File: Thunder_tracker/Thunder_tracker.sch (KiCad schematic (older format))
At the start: 5 parts, among them U1 ATmega8A-PU, U2 RFM95W-868S2

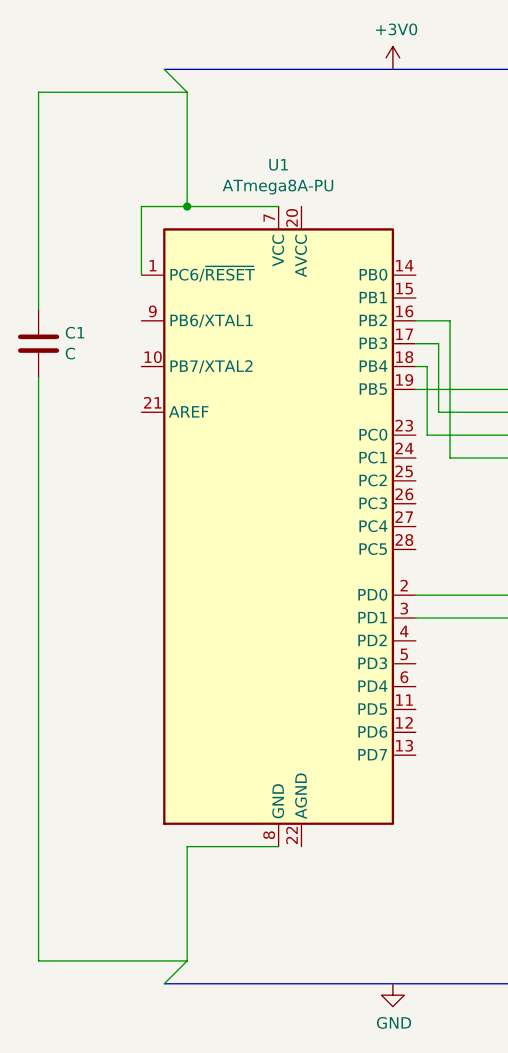
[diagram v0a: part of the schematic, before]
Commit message: Updated schematics. Now we'll use an external 32.768KHz crystal.
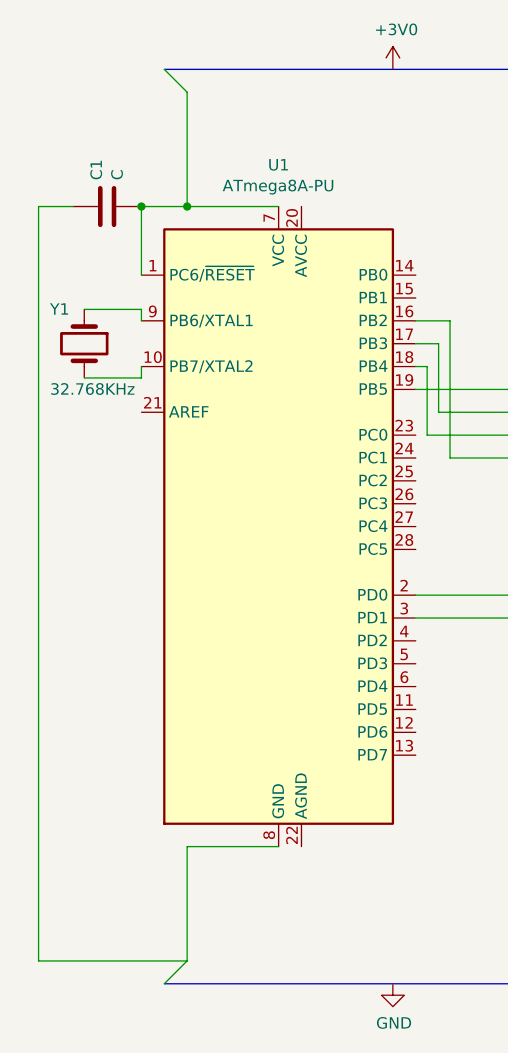
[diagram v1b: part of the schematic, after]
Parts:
- added Y1: 32.768KHz, symbol Device:Crystal
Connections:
- net at U1.1 (PC6/~RESET), U1.7 (VCC): now also C1.2; no longer C1.1
- net at U1.10 (PB7/XTAL2): now also Y1.2
- net at U1.8 (GND): now also C1.1; no longer C1.2
- net at U1.9 (PB6/XTAL1): now also Y1.1
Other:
- moved on the sheet: C1
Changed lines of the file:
@@
 L Device:C C1
 U 1 1 5D9B5CBD
-P 3000 2050
-F 0 "C1" H 3115 2096 50  0000 L CNN
-F 1 "C" H 3115 2005 50  0000 L CNN
-F 2 "" H 3038 1900 50  0001 C CNN
-F 3 "~" H 3000 2050 50  0001 C CNN
-	1    3000 2050
-	1    0    0    -1
+P 3300 1450
+F 0 "C1" H 3415 1496 50  0000 L CNN
+F 1 "C" H 3415 1405 50  0000 L CNN
+F 2 "" H 3338 1300 50  0001 C CNN
+F 3 "~" H 3300 1450 50  0001 C CNN
+	1    3300 1450
+	0    -1   -1   0
 $EndComp
 Wire Wire Line
-	3000 2200 3000 4750
-Wire Wire Line
 	3000 4750 3650 4750
-Wire Wire Line
-	3000 1900 3000 950
-Wire Wire Line
-	3000 950  3650 950
 $Comp
 L Device:C C2
@@
 	0    1    1    0
 $EndComp
+Connection ~ 3450 1450
+Wire Wire Line
+	3150 1450 3000 1450
+Wire Wire Line
+	3000 1450 3000 4750
+$Comp
+L Device:Crystal Y1
+U 1 1 5D9B7E9E
+P 3200 2050
+F 0 "Y1" V 3050 1900 50  0000 L CNN
+F 1 "32.768KHz" V 3400 1900 50  0000 L CNN
+F 2 "" H 3200 2050 50  0001 C CNN
+F 3 "~" H 3200 2050 50  0001 C CNN
+	1    3200 2050
+	0    1    1    0
+$EndComp
+Wire Wire Line
+	3200 2200 3450 2200
+Wire Wire Line
+	3450 2200 3450 2150
+Wire Wire Line
+	3200 1900 3450 1900
+Wire Wire Line
+	3450 1900 3450 1950
 Wire Bus Line
 	3550 4850 5550 4850
